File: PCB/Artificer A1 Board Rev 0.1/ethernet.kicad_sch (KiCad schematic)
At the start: 4 parts, among them U8 RTL8211F-CG, U9 RTL8211F-CG

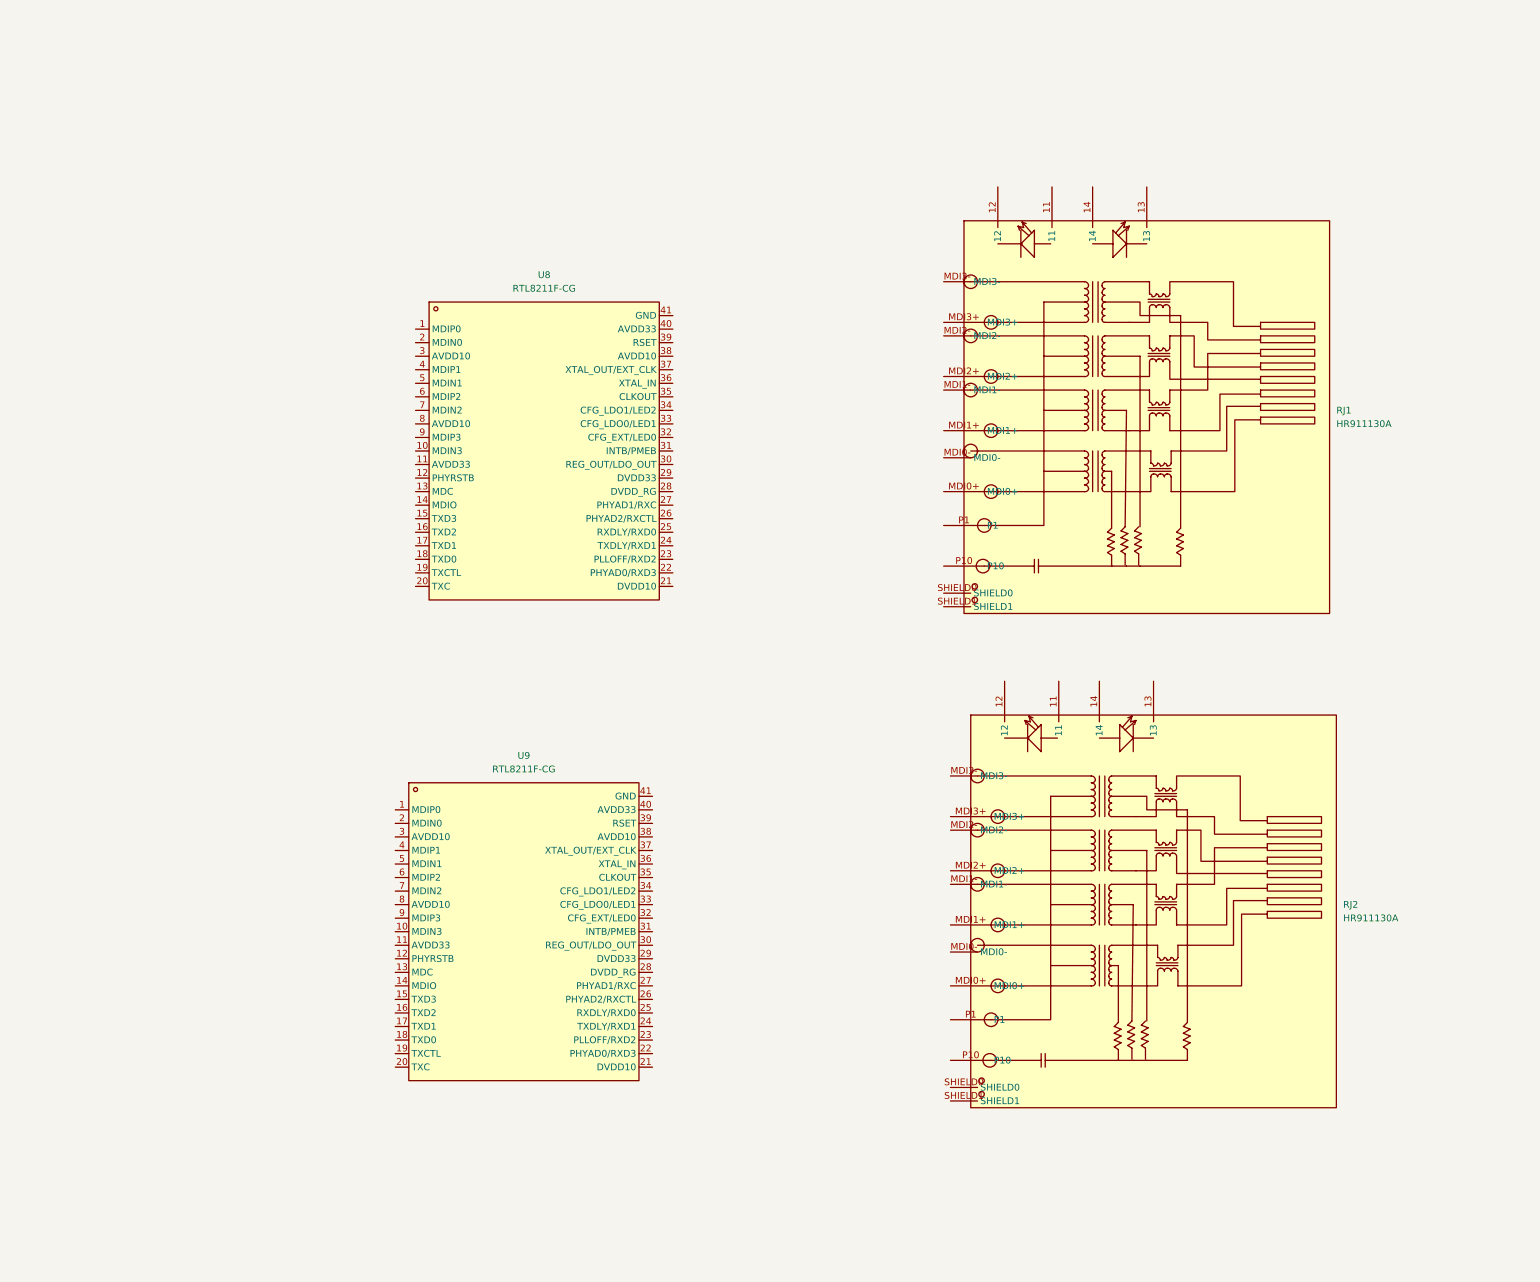
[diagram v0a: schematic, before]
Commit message: schematic update
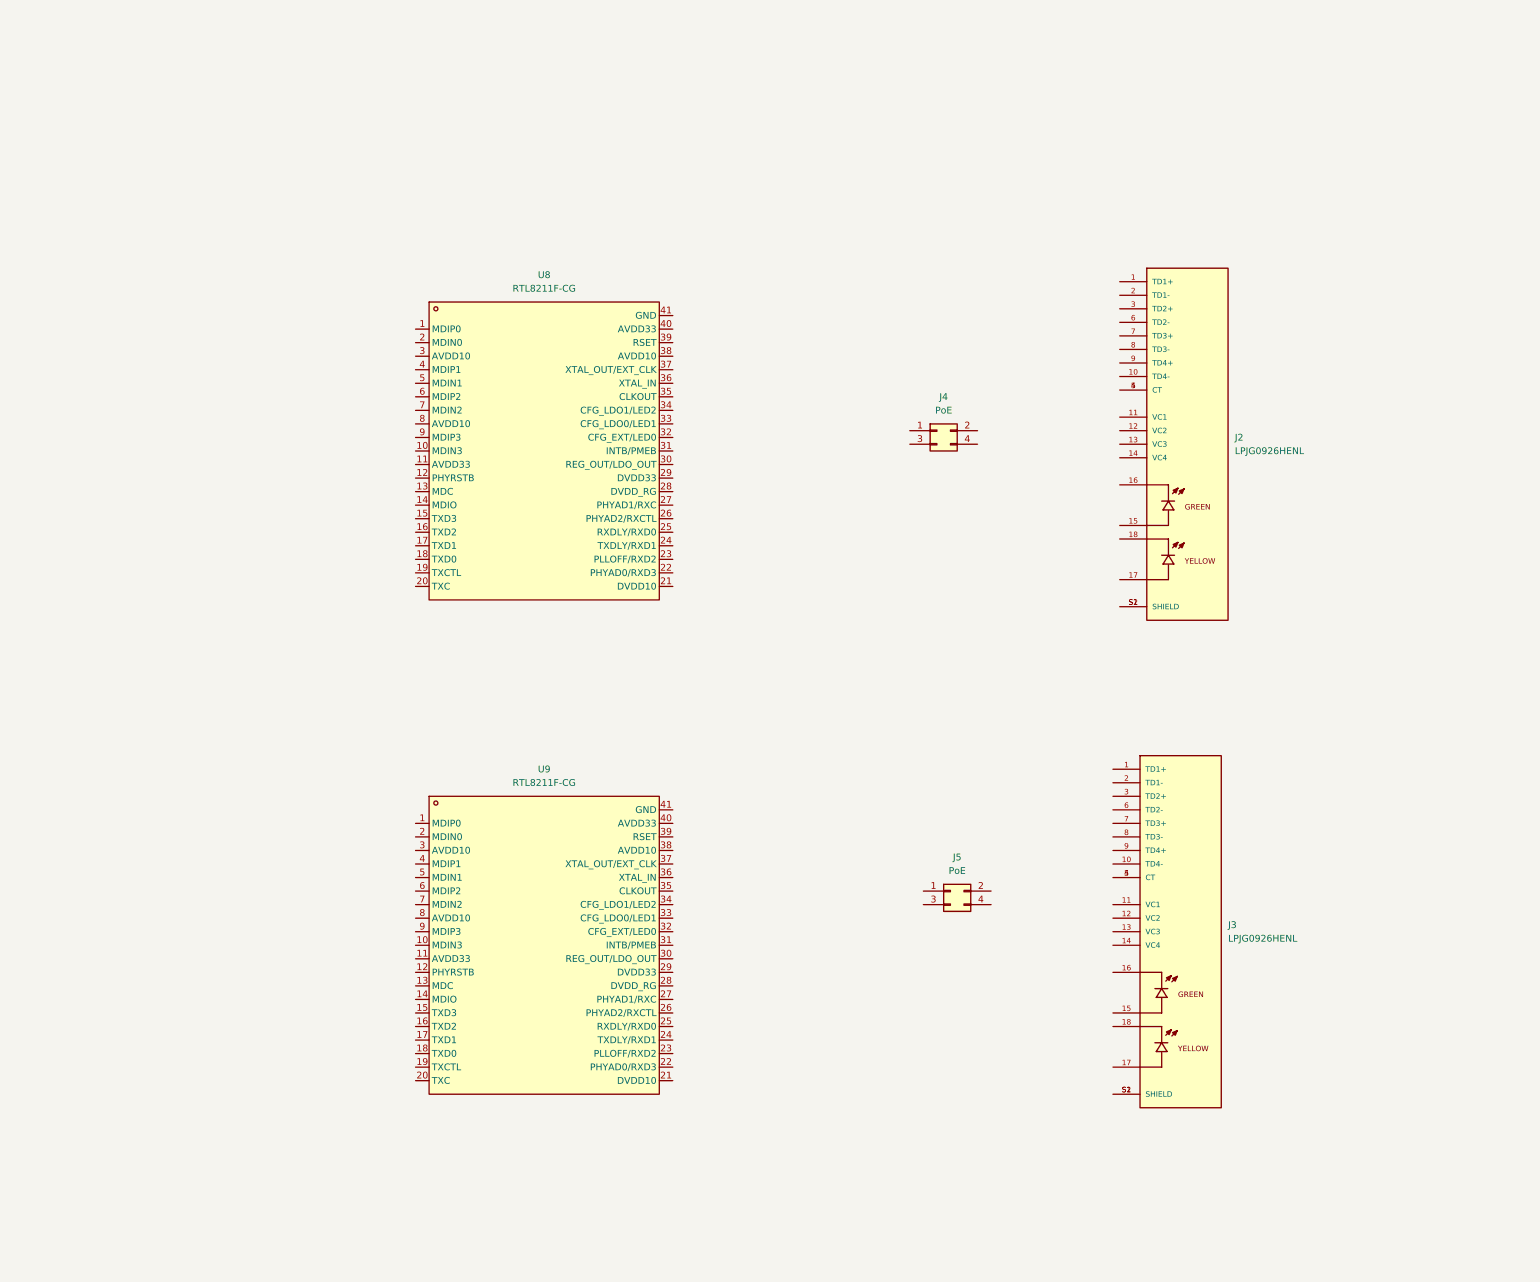
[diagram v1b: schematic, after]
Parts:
- removed RJ1, RJ2: HR911130A, easyeda2kicad:RJ45-TH_HR911130A, symbol easyeda2kicad:HR911130A
- added J2, J3: LPJG0926HENL, local_footprints:LINK-PP_LPJG0926HENL, symbol LPJG0926HENL:LPJG0926HENL
- added J4, J5: PoE, Connector_PinHeader_2.54mm:PinHeader_2x02_P2.54mm_Vertical, symbol Connector_Generic:Conn_02x02_Odd_Even
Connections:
- new net: J2.4 (CT), J2.5 (CT)
- new net: J2.S1 (SHIELD), J2.S2 (SHIELD)
- new net: J3.4 (CT), J3.5 (CT)
- new net: J3.S1 (SHIELD), J3.S2 (SHIELD)
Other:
- moved on the sheet: U9

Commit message: localized libraries
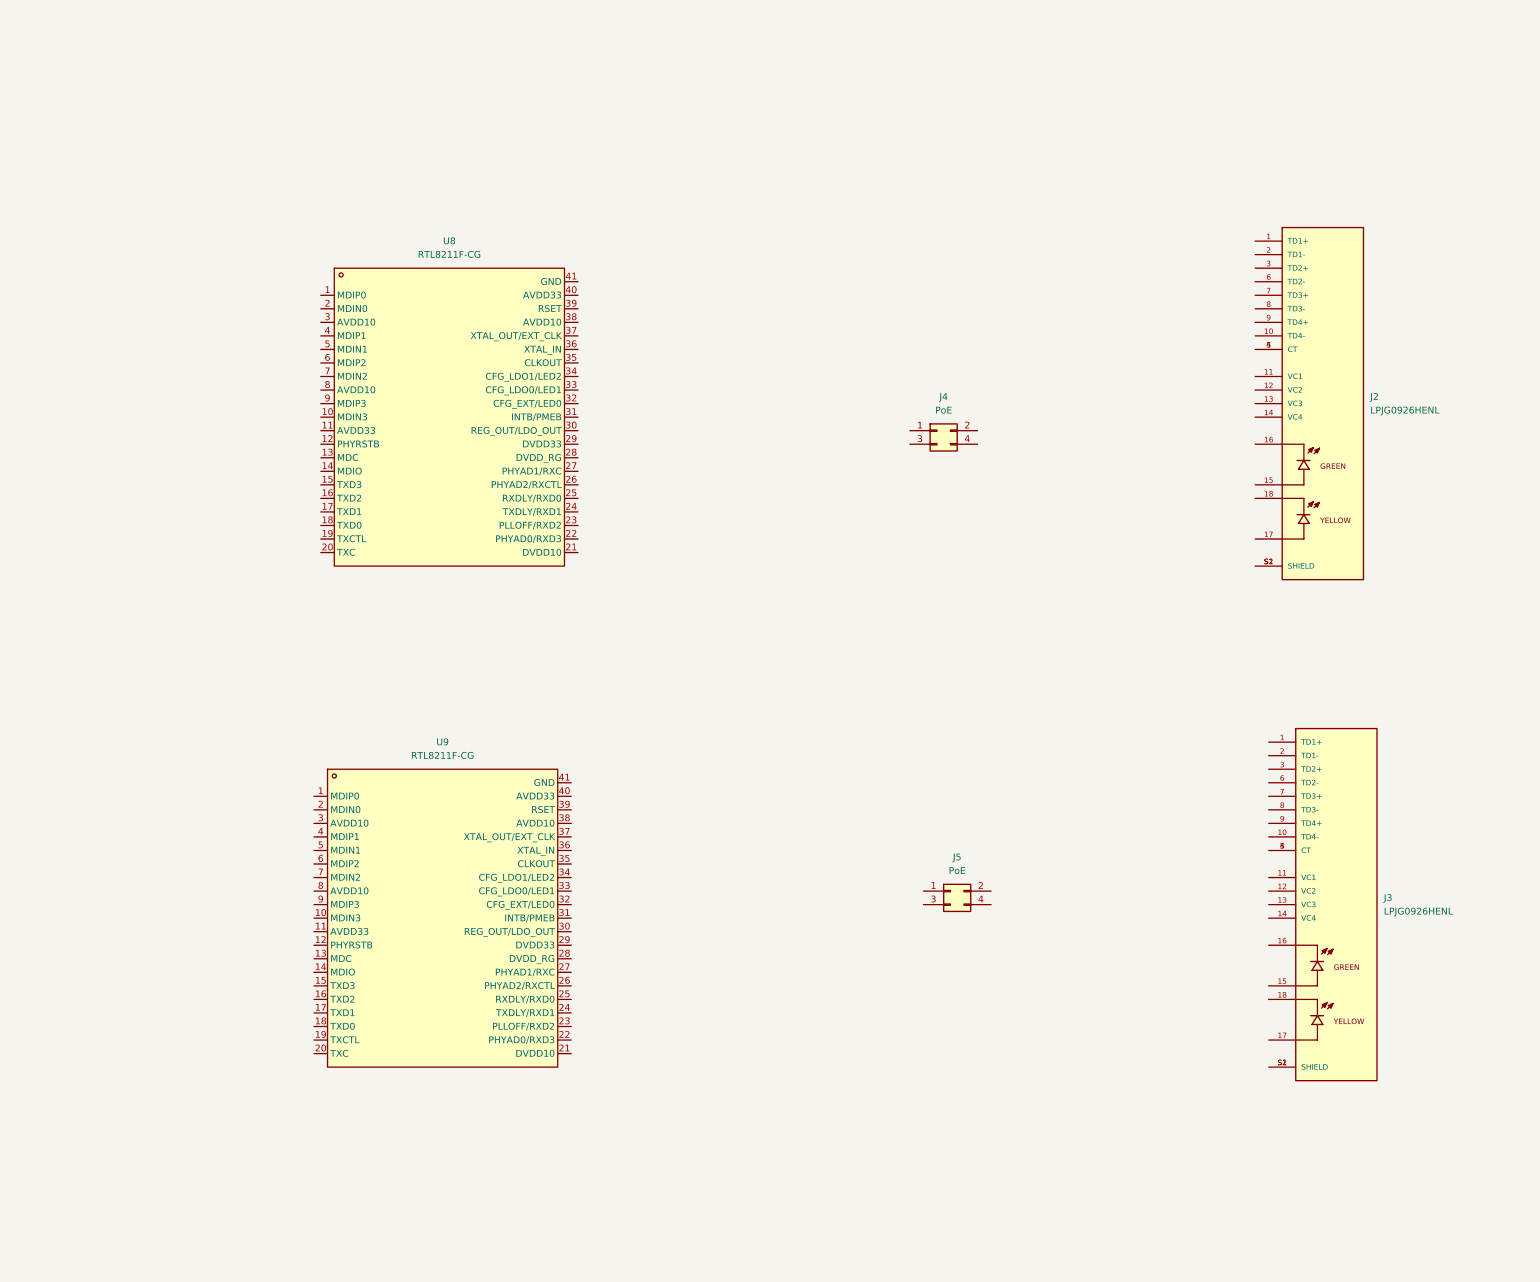
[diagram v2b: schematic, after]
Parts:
- removed U8, U9: RTL8211F-CG, easyeda2kicad:WQFN-40_L5.0-W5.0-P0.4-BL-EP, symbol easyeda2kicad:RTL8211F-CG
- added U8, U9: RTL8211F-CG, easyeda:WQFN-40_L5.0-W5.0-P0.4-BL-EP, symbol easyeda symbols:RTL8211F-CG
- J2, J3: footprint local_footprints:LINK-PP_LPJG0926HENL -> custom footprints:LINK-PP_LPJG0926HENL

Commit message: dc-dc & started eth PHY
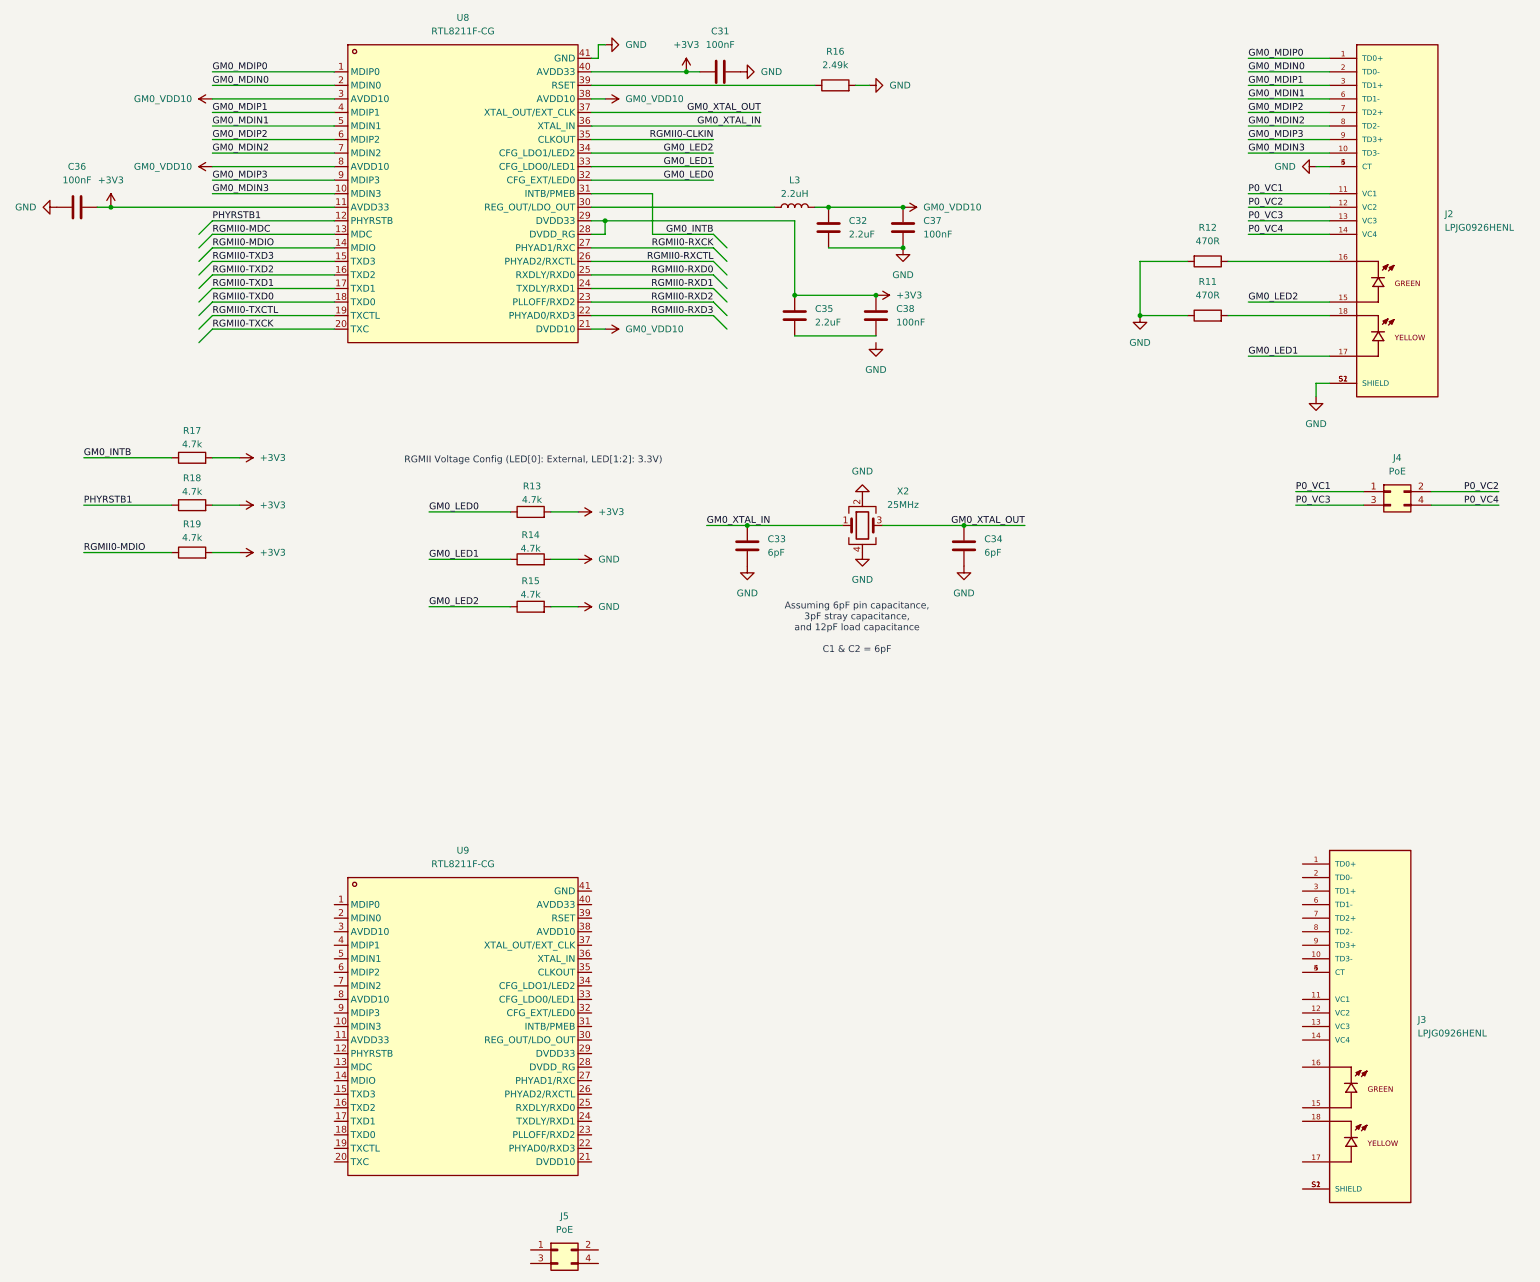
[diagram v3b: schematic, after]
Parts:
- added C31, C36, C37, C38: 100nF, symbol Device:C
- added C32, C35: 2.2uF, symbol Device:C
- added C33, C34: 6pF, symbol Device:C
- added L3: 2.2uH, symbol Device:L
- added R11, R12: 470R, symbol Device:R
- added R13, R14, R15, R17, R18, R19: 4.7k, symbol Device:R
- added R16: 2.49k, symbol Device:R
- added X2: 25MHz, Crystal:Crystal_SMD_2520-4Pin_2.5x2.0mm, symbol Device:Crystal_GND24
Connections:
- net GM0_MDIP0: now reaches J2.1 (TD0+)
- net GM0_MDIP0: now also U8.1 (MDIP0)
- net GM0_MDIN3: now reaches J2.10 (TD3-)
- net GM0_MDIN3: now also U8.10 (MDIN3)
- net P0_VC1: now reaches J2.11 (VC1)
- net P0_VC1: now also J4.1 (Pin_1)
- net P0_VC2: now reaches J2.12 (VC2)
- net P0_VC2: now also J4.2 (Pin_2)
- net P0_VC3: now reaches J2.13 (VC3)
- net P0_VC3: now also J4.3 (Pin_3)
- net P0_VC4: now reaches J2.14 (VC4)
- net P0_VC4: now also J4.4 (Pin_4)
- net GM0_LED2: now reaches J2.15
- net GM0_LED2: now also U8.34 (CFG_LDO1/LED2), R15.1
- net at J2.16: now also R12.1
- net GM0_LED1: now reaches J2.17
- net GM0_LED1: now also U8.33 (CFG_LDO0/LED1), R14.1
- net at J2.18: now also R11.2
- net GM0_MDIN0: now reaches J2.2 (TD0-)
- net GM0_MDIN0: now also U8.2 (MDIN0)
- net GM0_MDIP1: now reaches J2.3 (TD1+)
- net GM0_MDIP1: now also U8.4 (MDIP1)
- net GND: now reaches J2.4 (CT), J2.5 (CT)
- net GND: now also J2.S1 (SHIELD), J2.S2 (SHIELD), U8.41 (GND), C31.2, C32.2, C33.2, C34.2, C36.2, C37.2, R11.1, R12.2, R14.2, R15.2, R16.2, X2.2, X2.4
- net GM0_MDIN1: now reaches J2.6 (TD1-)
- net GM0_MDIN1: now also U8.5 (MDIN1)
- net GM0_MDIP2: now reaches J2.7 (TD2+)
- net GM0_MDIP2: now also U8.6 (MDIP2)
- net GM0_MDIN2: now reaches J2.8 (TD2-)
- net GM0_MDIN2: now also U8.7 (MDIN2)
- net GM0_MDIP3: now reaches J2.9 (TD3+)
- net GM0_MDIP3: now also U8.9 (MDIP3)
- net +3V3: now reaches U8.11 (AVDD33)
- net +3V3: now also U8.28 (DVDD_RG), U8.29 (DVDD33), U8.40 (AVDD33), C31.1, C35.1, C36.1, C38.1, R13.2, R17.2, R18.2, R19.2
- net PHYRSTB1: now reaches U8.12 (PHYRSTB)
- net PHYRSTB1: now also R18.1
- net RGMII0-MDC: now reaches U8.13 (MDC)
- net RGMII0-MDIO: now reaches U8.14 (MDIO)
- net RGMII0-MDIO: now also R19.1
- net RGMII0-TXD3: now reaches U8.15 (TXD3)
- net RGMII0-TXD2: now reaches U8.16 (TXD2)
- net RGMII0-TXD1: now reaches U8.17 (TXD1)
- net RGMII0-TXD0: now reaches U8.18 (TXD0)
- net RGMII0-TXCTL: now reaches U8.19 (TXCTL)
- net RGMII0-TXCK: now reaches U8.20 (TXC)
- net GM0_VDD10: now reaches U8.21 (DVDD10)
- net GM0_VDD10: now also U8.3 (AVDD10), U8.38 (AVDD10), U8.8 (AVDD10), C32.1, C37.1, L3.2
- net RGMII0-RXD3: now reaches U8.22 (PHYAD0/RXD3)
- net RGMII0-RXD2: now reaches U8.23 (PLLOFF/RXD2)
- net RGMII0-RXD1: now reaches U8.24 (TXDLY/RXD1)
- net RGMII0-RXD0: now reaches U8.25 (RXDLY/RXD0)
- net RGMII0-RXCTL: now reaches U8.26 (PHYAD2/RXCTL)
- net RGMII0-RXCK: now reaches U8.27 (PHYAD1/RXC)
- net at U8.30 (REG_OUT/LDO_OUT): now also L3.1
- net GM0_INTB: now reaches U8.31 (INTB/PMEB)
- net GM0_INTB: now also R17.1
- net GM0_LED0: now reaches U8.32 (CFG_EXT/LED0)
- net GM0_LED0: now also R13.1
- net RGMII0-CLKIN: now reaches U8.35 (CLKOUT)
- net GM0_XTAL_IN: now reaches U8.36 (XTAL_IN)
- net GM0_XTAL_IN: now also C33.1, X2.1
- net GM0_XTAL_OUT: now reaches U8.37 (XTAL_OUT/EXT_CLK)
- net GM0_XTAL_OUT: now also C34.1, X2.3
- net at U8.39 (RSET): now also R16.1
- new net: C35.2, C38.2
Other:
- note added: "Assuming 6pF pin capacitance, 3pF stray capacitance, and 12pF load capacitance C1 & C2 = 6pF"
- note added: "RGMII Voltage Config (LED[0]: External, LED[1:2]: 3.3V)"
- moved on the sheet: J2, J3, J4, J5, U8, U9
